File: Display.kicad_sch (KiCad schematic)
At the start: 6 parts, among them U2 HPDL1414, U3 HPDL1414, U4 HPDL1414, U5 HPDL1414, U7 74AHC595

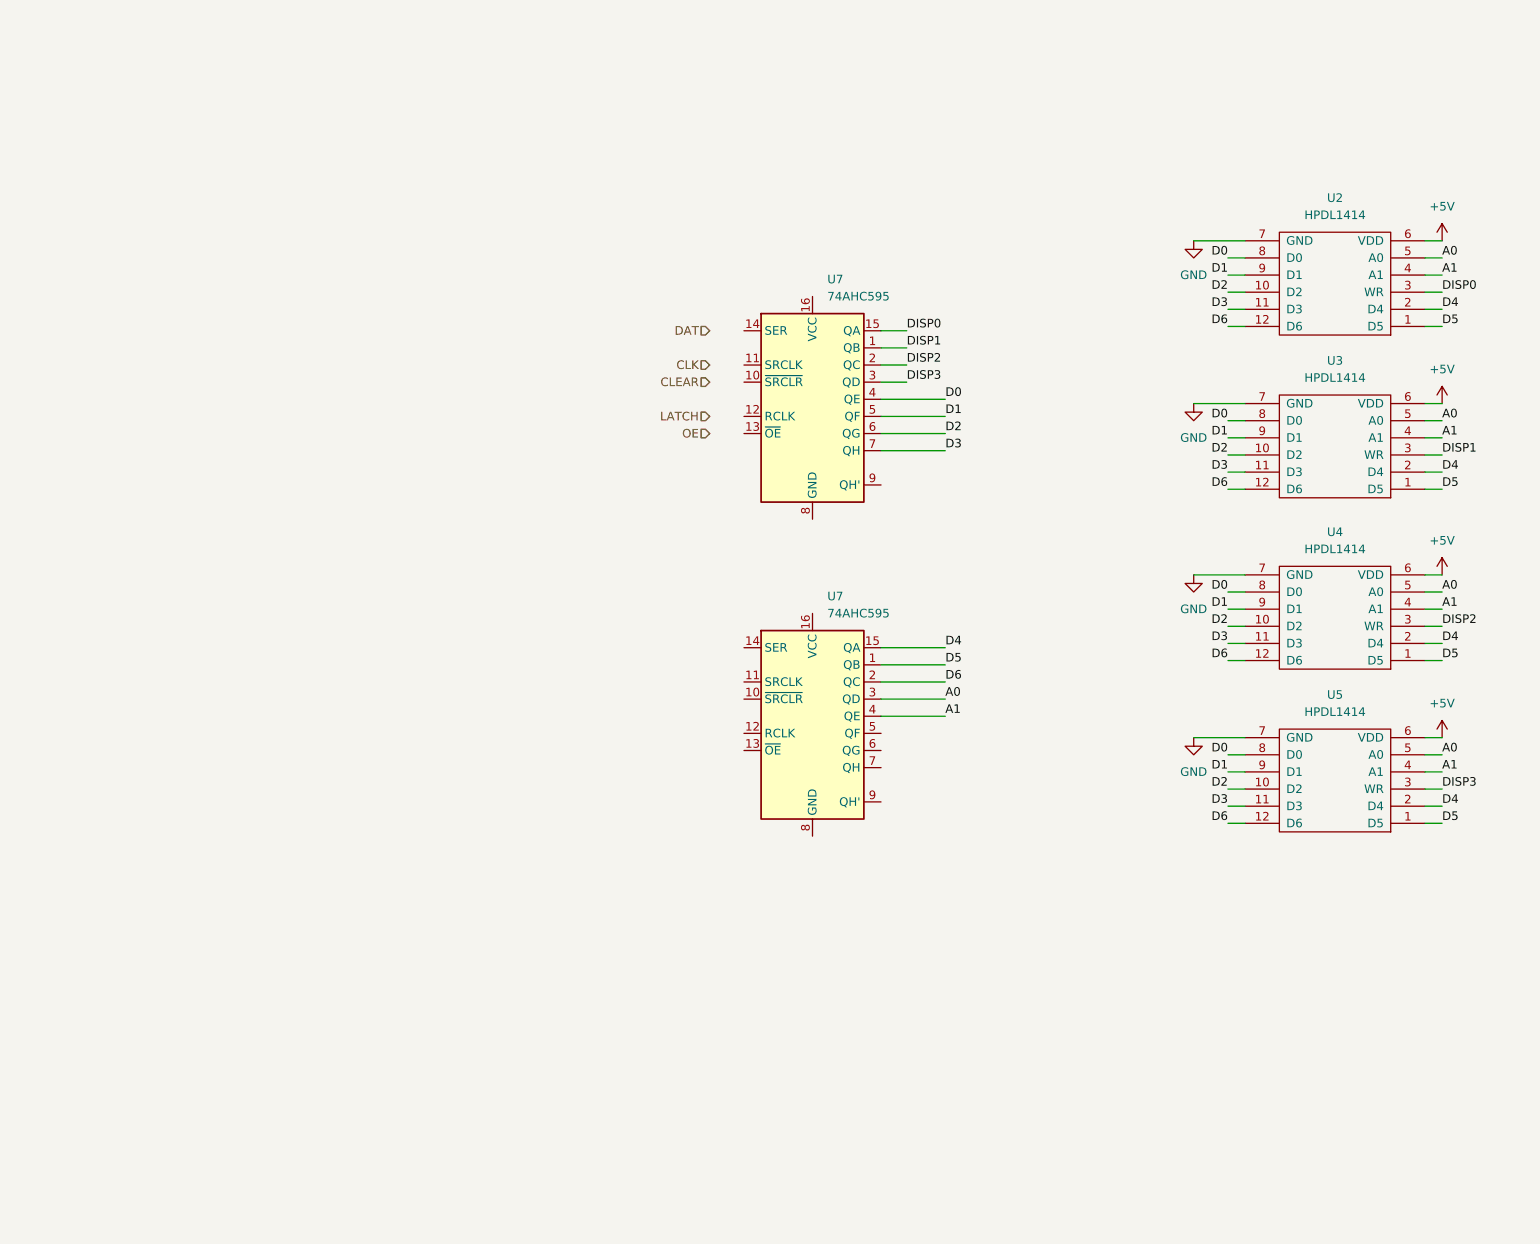
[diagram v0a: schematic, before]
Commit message: Begin screen module
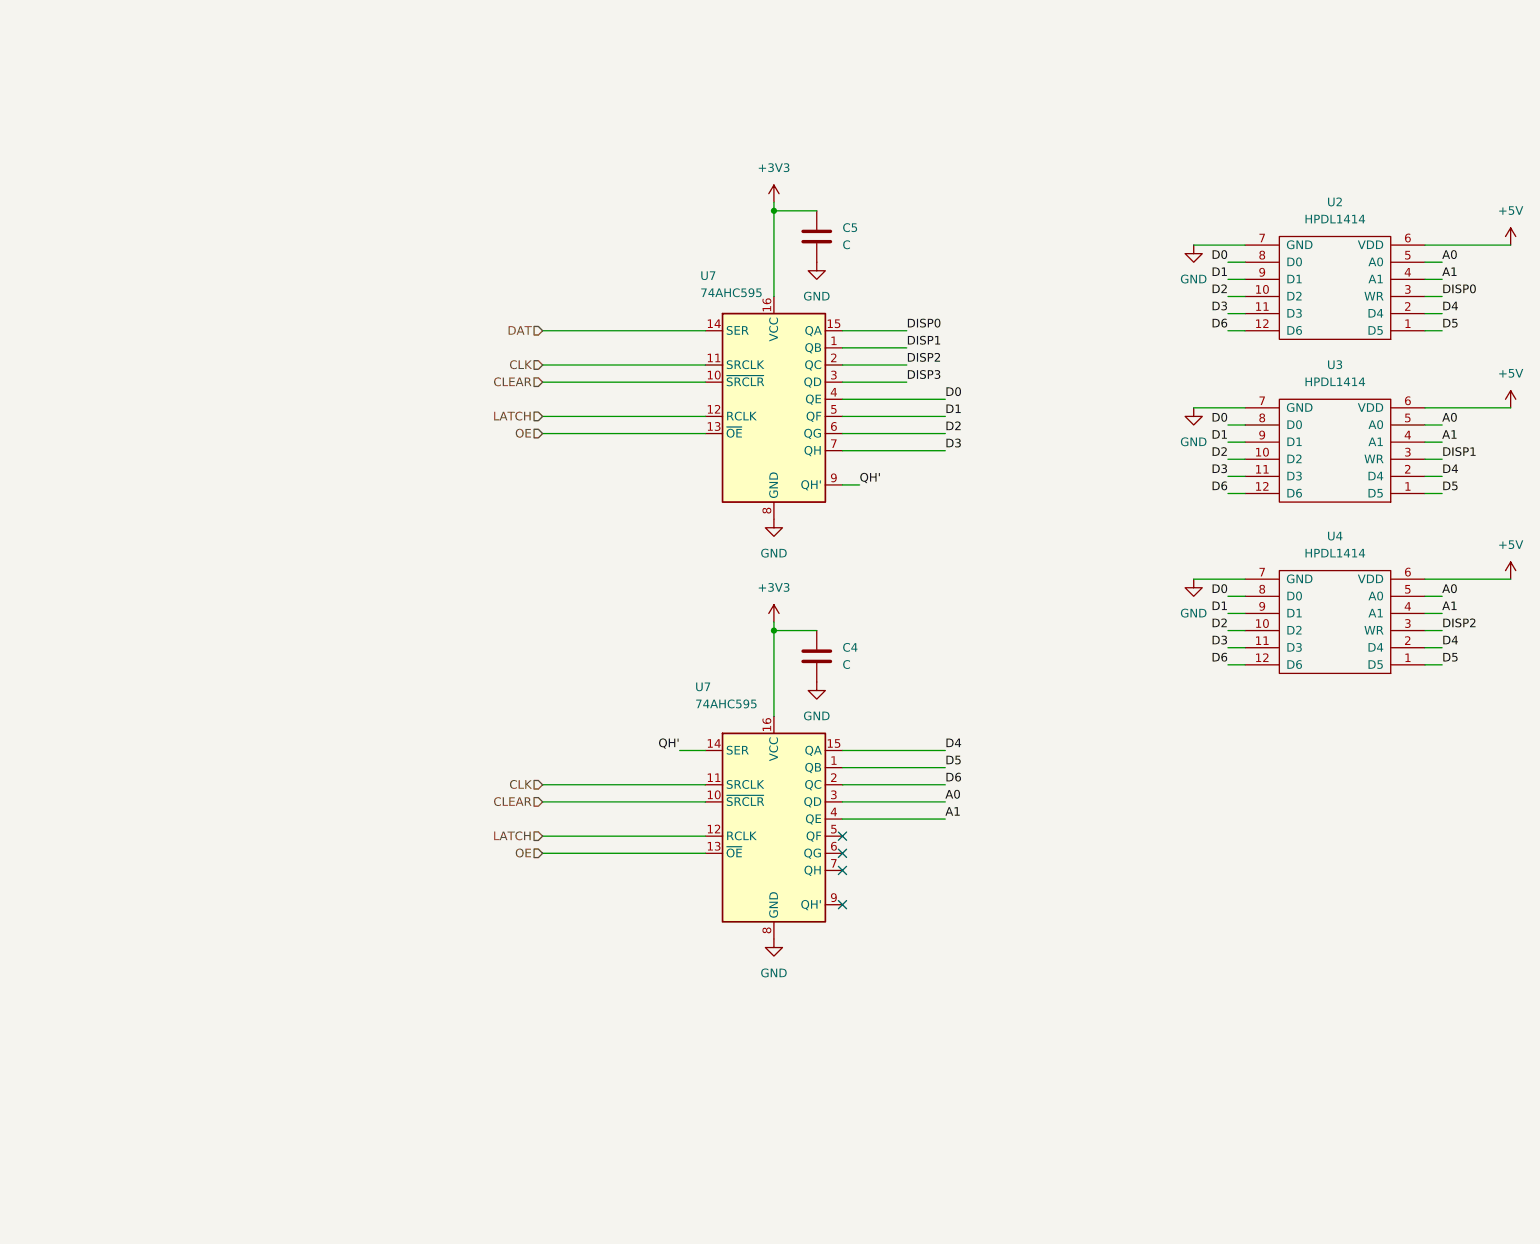
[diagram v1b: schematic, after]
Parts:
- removed U5: HPDL1414, DL1414:HPDLDL-1414, symbol DL1414:HPDL1414
- added C4, C5: C, symbol Device:C
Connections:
- net CLEAR: now also U7.10 (~{SRCLR}), U7.10 (~{SRCLR})
- net CLK: now also U7.11 (SRCLK), U7.11 (SRCLK)
- net DAT: now also U7.14 (SER)
- net GND: now also U7.8 (GND), U7.8 (GND), C4.2, C5.2
- net LATCH: now also U7.12 (RCLK), U7.12 (RCLK)
- net OE: now also U7.13 (~{OE}), U7.13 (~{OE})
- net +3V3: now reaches U7.16 (VCC)
- net +3V3: now also U7.16 (VCC), C4.1, C5.1
- net QH': now reaches U7.9 (QH')
- net QH': now also U7.14 (SER)
- no-connect marks 0 -> 4
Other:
- moved on the sheet: U2, U3, U4, U7

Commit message: Update
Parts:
- removed U2, U3, U4: HPDL1414, DL1414:HPDLDL-1414, symbol DL1414:HPDL1414
- added C11: 1u, symbol Device:C
- added R10, R11, R12, R13, R3, R4, R8, R9: 510R, symbol Device:R
- added U4: ~, footprints:display, symbol project parts:display
- added U7: 74AHC595, symbol 74xx:74AHC595
- C4, C5: value C -> 1u
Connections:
- net +3V3: now also C11.1, U7.16 (VCC)
- net CLEAR: now also U7.10 (~{SRCLR})
- net CLK: now also U7.11 (SRCLK)
- net GND: now also C11.2, U7.8 (GND)
- net LATCH: now also U7.12 (RCLK)
- net OE: now also U7.13 (~{OE})
- net G6: now reaches U7.5 (QF)
- net G6: now also U4.14 (G6)
- net G7: now reaches U7.6 (QG)
- net G7: now also U4.15 (G7)
- net G8: now reaches U7.7 (QH)
- net G8: now also U4.16 (G8)
- net QH'1: now reaches U7.9 (QH')
- net QH'1: now also U7.14 (SER)
- net A0 renamed G4
- net G4: now also U4.12 (G4)
- net A1 renamed G5
- net G5: now also U4.13 (G5)
- net D0: no longer names the net of U7.4 (QE)
- net D0: now also R10.1
- net D1: no longer names the net of U7.5 (QF)
- net D1: now also R11.1
- net D2: no longer names the net of U7.6 (QG)
- net D2: now also R12.1
- net D3: no longer names the net of U7.7 (QH)
- net D3: now also R13.1
- net D4 renamed G1
- net G1: now also U4.9 (G1)
- net D5 renamed G2
- net G2: now also U4.10 (G2)
- net D6 renamed G3
- net G3: now also U4.11 (G3)
- net DISP0: no longer names the net of U7.15 (QA)
- net DISP0: now also R3.1
- net DISP1: no longer names the net of U7.1 (QB)
- net DISP1: now also R4.1
- net DISP2: no longer names the net of U7.2 (QC)
- net DISP2: now also R8.1
- net DISP3: no longer names the net of U7.3 (QD)
- net DISP3: now also R9.1
- net QH' renamed QH'0
- new net: R10.2, U4.2 (E)
- new net: R12.2, U4.3 (G)
- new net: R8.2, U4.7 (C)
- new net: R11.2, U4.4 (F)
- new net: R13.2, U4.8 (DP)
- new net: R9.2, U4.1 (D)
- new net: R3.2, U4.5 (A)
- new net: R4.2, U4.6 (B)
- new net G10: U4.18 (G10), U7.1 (QB)
- new net G11: U4.19 (G11), U7.2 (QC)
- new net G12: U4.20 (G12), U7.3 (QD)
- new net G9: U4.17 (G9), U7.15 (QA)
- no-connect marks 4 -> 5
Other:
- moved on the sheet: C4, C5, U7
